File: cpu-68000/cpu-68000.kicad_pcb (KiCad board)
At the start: 4 copper layers, 160 x 100 mm, 114 parts, among them J101 Conn_02x04_Odd_Even, J201 Conn_03x32_Row_Letter_First, J502 DB9_Male_MountingHoles, J503 Conn_02x03_Odd_Even, SW501 SW_DIP_x05, SW502 Blue, SW503 Black, U101 ATF22V10C, U102 ATF22V10C, U103 74HC175, U104 74HC05, U201 SN74LVCH16T245, U202 SN74LVCH16T245, U203 SN74LXC8T245, U204 SN74LVC2T45, U205 SN74LVC2T45, U301 MC68000FN, U303 TL7733B, U304 74HC175, U305 ATF22V10C, U306 74HC148, U401 SST39SF040, U402 SST39SF040, U403 IS61C5128AL-10TLI, U404 IS61C5128AL-10TLI, U501 74HC14, U502 74HC245, U503 XR68C681, U504 PCF8584, U505 DS1744, U506 MAX202, X101 10MHz, Y501 3.6864MHz

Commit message: Placed most items on pcb
- Laid out most components where they should go on the board; mostly
  routed the connector side of the bus buffers and the address bus

- Added 3d models for PLCC sockets, RTC clock module
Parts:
- removed R101: 1k, Resistor_SMD:R_0805_2012Metric
- removed R202: 5k, Resistor_SMD:R_0805_2012Metric
- added R507: 10k, Resistor_SMD:R_0805_2012Metric, F.Cu at (168.2, 107.5)
- added TP201: TestPoint, TestPoint:TestPoint_Loop_D2.60mm_Drill1.4mm_Beaded, F.Cu at (55.2, 115.0)
- added TP202: TestPoint, TestPoint:TestPoint_Loop_D2.60mm_Drill1.4mm_Beaded, F.Cu at (60.7, 115.0)
- D201: value LED_Dual_AAKK -> Grn; footprint 68komputer-common:H201Cxx -> 68komputer-common:H100Cxx
- RN501: footprint Resistor_THT:R_Array_SIP8 -> Resistor_SMD:R_Array_Convex_4x1206
- RN502: value 10k -> R_Network05; footprint Resistor_THT:R_Array_SIP9 -> Resistor_THT:R_Array_SIP6
- U401, U402: value SST39SF040 -> SST39SF040-55-4C; footprint Package_LCC:PLCC-32_THT-Socket -> Package_SO:TSOP-I-32_11.8x8mm_P0.5mm
- moved U505 259.7 mm to (121.5, 108.8), turned to 90 degrees
- moved R201 252.5 mm to (168.9, 28.5)
- moved C505 251.0 mm to (165.2, 127.0)
- moved C509 251.0 mm to (160.8, 127.0)
- moved C506 251.0 mm to (165.2, 124.0)
- moved C507 251.0 mm to (160.8, 124.0)
- moved C508 232.5 mm to (153.3, 123.9)
- moved C510 232.5 mm to (153.3, 126.9)
- moved RN502 228.8 mm to (166.5, 59.2), turned to -90 degrees
- moved C511 228.8 mm to (142.9, 125.3)
- moved Y501 225.7 mm to (120.0, 79.8), turned to 90 degrees
- moved R501 224.3 mm to (148.6, 125.8)
- moved R502 221.0 mm to (138.2, 124.2)
- moved C503 220.1 mm to (124.3, 80.7), turned to 90 degrees
- moved U503 219.0 mm to (136.7, 80.2), turned to 180 degrees
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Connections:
- D201 pad 1: Net-(D201-Pad1) -> GND
- J201 pad a10: /Backplane Connection/BD1 -> GND
- J201 pad a11: /Backplane Connection/BD2 -> /Backplane Connection/BD14
- J201 pad a12: /Backplane Connection/BD3 -> GND
- J201 pad a13: GND -> /Backplane Connection/BA23
- J201 pad a14: /Backplane Connection/BD4 -> GND
- J201 pad a15: /Backplane Connection/BD5 -> /Backplane Connection/BA20
- J201 pad a16: /Backplane Connection/BD6 -> /Backplane Connection/BA13
- J201 pad a17: /Backplane Connection/BD7 -> /Backplane Connection/BA14
- J201 pad a18: GND -> /Backplane Connection/BA11
- J201 pad a19: unconnected-(J201-Pada19) -> GND
- J201 pad a20: unconnected-(J201-Pada20) -> /Backplane Connection/BA7
- J201 pad a21: unconnected-(J201-Pada21) -> /Backplane Connection/BA5
- J201 pad a22: unconnected-(J201-Pada22) -> /Backplane Connection/BR/~{W}
- J201 pad a23: /Backplane Connection/BA1 -> unconnected-(J201-Pada23)
- J201 pad a24: /Backplane Connection/BA3 -> unconnected-(J201-Pada24)
- J201 pad a25: GND -> unconnected-(J201-Pada25)
- J201 pad a26: /Backplane Connection/BA8 -> unconnected-(J201-Pada26)
- J201 pad a27: /Backplane Connection/BA11 -> unconnected-(J201-Pada27)
- J201 pad a28: /Backplane Connection/BA13 -> unconnected-(J201-Pada28)
- J201 pad a29: /Backplane Connection/BA15 -> unconnected-(J201-Pada29)
- J201 pad a3: GND -> /I2C_SCL
- J201 pad a30: GND -> unconnected-(J201-Pada30)
- J201 pad a31: /Backplane Connection/BA18 -> /~{RESET}
- J201 pad a32: /Backplane Connection/BA21 -> /~{IACK_EXT}
- J201 pad a4: /~{BR} -> GND
- J201 pad a5: /I2C_SCL -> GND
- J201 pad a6: /~{IRQ_EXT} -> /Backplane Connection/BD2
- J201 pad a7: /Backplane Connection/BR/~{W} -> /Backplane Connection/BD5
- J201 pad a8: GND -> /Backplane Connection/BD8
- J201 pad a9: /Backplane Connection/BD0 -> /Backplane Connection/BD10
- J201 pad b10: /Backplane Connection/BD10 -> /Backplane Connection/BD12
- J201 pad b11: /Backplane Connection/BD11 -> /Backplane Connection/BD15
- J201 pad b13: /Backplane Connection/BD12 -> GND
- J201 pad b14: /Backplane Connection/BD13 -> /Backplane Connection/BA21
- J201 pad b15: /Backplane Connection/BD14 -> /Backplane Connection/BA15
- J201 pad b16: /Backplane Connection/BD15 -> /Backplane Connection/BA16
- J201 pad b17: GND -> /Backplane Connection/BA10
- J201 pad b18: unconnected-(J201-Padb18) -> GND
- J201 pad b19: unconnected-(J201-Padb19) -> /Backplane Connection/BA9
- J201 pad b20: unconnected-(J201-Padb20) -> /Backplane Connection/BA4
- J201 pad b21: unconnected-(J201-Padb21) -> /Backplane Connection/BA3
- J201 pad b22: unconnected-(J201-Padb22) -> /Backplane Connection/~{BAS}
- J201 pad b24: GND -> unconnected-(J201-Padb24)
- J201 pad b25: /Backplane Connection/BA5 -> unconnected-(J201-Padb25)
- J201 pad b26: /Backplane Connection/BA7 -> unconnected-(J201-Padb26)
- J201 pad b27: /Backplane Connection/BA10 -> unconnected-(J201-Padb27)
- J201 pad b28: /Backplane Connection/BA12 -> unconnected-(J201-Padb28)
- J201 pad b29: GND -> unconnected-(J201-Padb29)
- J201 pad b30: /Backplane Connection/BA17 -> unconnected-(J201-Padb30)
- J201 pad b31: /Backplane Connection/BA19 -> GND
- J201 pad b32: /Backplane Connection/BA22 -> /~{IRQ_EXT}
- J201 pad b4: /~{BG} -> GND
- J201 pad b5: /~{EXT_BERR} -> /Backplane Connection/BD0
- J201 pad b6: /~{RESET} -> /Backplane Connection/BD3
- J201 pad b7: GND -> /Backplane Connection/BD6
- J201 pad b8: /Backplane Connection/BD8 -> /Backplane Connection/BD9
- J201 pad b9: /Backplane Connection/BD9 -> GND
- J201 pad c10: /~{DTACK} -> /Backplane Connection/BD13
- J201 pad c12: unconnected-(J201-Padc12) -> /Backplane Connection/BA22
- J201 pad c13: unconnected-(J201-Padc13) -> /Backplane Connection/BA19
- J201 pad c14: unconnected-(J201-Padc14) -> /Backplane Connection/BA17
- J201 pad c15: unconnected-(J201-Padc15) -> /Backplane Connection/BA18
- J201 pad c16: unconnected-(J201-Padc16) -> /Backplane Connection/BA12
- J201 pad c17: unconnected-(J201-Padc17) -> GND
- J201 pad c18: unconnected-(J201-Padc18) -> /Backplane Connection/BA8
- J201 pad c19: unconnected-(J201-Padc19) -> /Backplane Connection/BA6
- J201 pad c20: unconnected-(J201-Padc20) -> /Backplane Connection/BA2
- J201 pad c21: unconnected-(J201-Padc21) -> /Backplane Connection/BA1
- J201 pad c22: unconnected-(J201-Padc22) -> /Backplane Connection/~{BLDS}
- J201 pad c23: unconnected-(J201-Padc23) -> /Backplane Connection/~{BUDS}
- J201 pad c24: /Backplane Connection/BA2 -> unconnected-(J201-Padc24)
- J201 pad c25: /Backplane Connection/BA4 -> unconnected-(J201-Padc25)
- J201 pad c26: /Backplane Connection/BA6 -> unconnected-(J201-Padc26)
- J201 pad c27: /Backplane Connection/BA9 -> unconnected-(J201-Padc27)
- J201 pad c28: GND -> unconnected-(J201-Padc28)
- J201 pad c29: /Backplane Connection/BA14 -> unconnected-(J201-Padc29)
- J201 pad c3: GND -> /I2C_SDA
- J201 pad c30: /Backplane Connection/BA16 -> unconnected-(J201-Padc30)
- J201 pad c31: /Backplane Connection/BA20 -> /~{DTACK}
- J201 pad c32: /Backplane Connection/BA23 -> /~{EXT_BERR}
- J201 pad c4: /~{BGACK} -> GND
- J201 pad c5: /I2C_SDA -> /Backplane Connection/BD1
- J201 pad c6: /~{IACK_EXT} -> /Backplane Connection/BD4
- J201 pad c7: /Backplane Connection/~{BLDS} -> /Backplane Connection/BD7
- J201 pad c8: /Backplane Connection/~{BUDS} -> GND
- J201 pad c9: /Backplane Connection/~{BAS} -> /Backplane Connection/BD11
- R201 pad 2: Net-(D201-Pad1) -> Net-(D201-Pad2)
- RN301 pad 2: /Main CPU/D7 -> /D7
- RN301 pad 3: /Main CPU/D6 -> /D6
- RN301 pad 4: /Main CPU/D5 -> /D5
- RN301 pad 5: /Main CPU/D4 -> /D4
- RN301 pad 6: /Main CPU/D3 -> /D3
- RN301 pad 7: /Main CPU/D2 -> /D2
- RN301 pad 8: /Main CPU/D1 -> /D1
- RN301 pad 9: /Main CPU/D0 -> /D0
- RN302 pad 2: /Main CPU/D15 -> /D15
- RN302 pad 3: /Main CPU/D14 -> /D14
- RN302 pad 4: /Main CPU/D13 -> /D13
- RN302 pad 5: /Main CPU/D12 -> /D12
- RN302 pad 6: /Main CPU/D11 -> /D11
- RN302 pad 7: /Main CPU/D10 -> /D10
- RN302 pad 8: /Main CPU/D9 -> /D9
- RN302 pad 9: /Main CPU/D8 -> /D8
- RN501 pad 1: Net-(D502-Pad1) -> Net-(D502-Pad2)
- RN501 pad 2: /Peripherals/LED3 -> Net-(D502-Pad1)
- RN501 pad 3: Net-(D502-Pad2) -> Net-(D501-Pad2)
- RN501 pad 4: /Peripherals/LED2 -> Net-(D501-Pad1)
- RN501 pad 5: Net-(D501-Pad2) -> /Peripherals/LED0
- RN501 pad 7: Net-(D501-Pad1) -> /Peripherals/LED2
- RN501 pad 8: /Peripherals/LED0 -> /Peripherals/LED3
- RN502 pad 2: /Peripherals/~{UART_CTS} -> /ROM_REMAP
- RN502 pad 3: unconnected-(RN502-Pad3) -> /Peripherals/DIPSW3
- RN502 pad 4: unconnected-(RN502-Pad4) -> /Peripherals/DIPSW2
- RN502 pad 5: /Peripherals/DIPSW0 -> /Peripherals/DIPSW1
- RN502 pad 6: /Peripherals/DIPSW1 -> /Peripherals/DIPSW0
- SW501 pad 1: /Peripherals/DIPSW0 -> +5V
- SW501 pad 10: +5V -> /Peripherals/DIPSW0
- SW501 pad 2: /Peripherals/DIPSW1 -> +5V
- SW501 pad 3: /Peripherals/DIPSW2 -> +5V
- SW501 pad 4: /Peripherals/DIPSW3 -> +5V
- SW501 pad 5: /ROM_REMAP -> +5V
- SW501 pad 6: +5V -> /ROM_REMAP
- SW501 pad 7: +5V -> /Peripherals/DIPSW3
- SW501 pad 8: +5V -> /Peripherals/DIPSW2
- SW501 pad 9: +5V -> /Peripherals/DIPSW1
- U101 pad 1: /~{UDS} -> unconnected-(U101-Pad1)
- U101 pad 10: unconnected-(U101-Pad10) -> /~{LDS}
- U101 pad 11: unconnected-(U101-Pad11) -> /~{AS}
- U101 pad 13: unconnected-(U101-Pad13) -> /~{UDS}
- U101 pad 2: /~{LDS} -> /~{EXT}
- U101 pad 3: /R/~{W} -> unconnected-(U101-Pad3)
- U101 pad 4: /~{AS} -> unconnected-(U101-Pad4)
- U101 pad 5: /~{MEM_EN} -> unconnected-(U101-Pad5)
- U101 pad 8: unconnected-(U101-Pad8) -> /R/~{W}
- U101 pad 9: unconnected-(U101-Pad9) -> /~{MEM_EN}
- U102 pad 1: /~{MEM_EN} -> unconnected-(U102-Pad1)
- U102 pad 11: unconnected-(U102-Pad11) -> /ROM_REMAP
- U102 pad 14: /~{ROM_CS} -> /~{PERIPH}
- U102 pad 15: /~{RAM_CS} -> /~{ROM_CS}
- U102 pad 16: /~{DUART_CS} -> /~{RAM_CS}
- U102 pad 17: /~{DISP_CS} -> /~{DUART_CS}
- U102 pad 18: /~{NVRAM_CS} -> /~{DISP_CS}
- U102 pad 19: /~{I2C_CS} -> /~{NVRAM_CS}
- U102 pad 20: /DTACK_FAST -> /~{I2C_CS}
- U102 pad 21: /DTACK_SLOW -> /DTACK_FAST
- U102 pad 22: /~{PERIPH} -> /DTACK_SLOW
- U102 pad 23: unconnected-(U102-Pad23) -> /~{EXT}
- U102 pad 6: /A19 -> unconnected-(U102-Pad6)
- U102 pad 8: /ROM_REMAP -> /A19
- U102 pad 9: unconnected-(U102-Pad9) -> /~{MEM_EN}
- U103 pad 10: Net-(J101-Pad4) -> Net-(J101-Pad6)
- U103 pad 12: Net-(J101-Pad6) -> Net-(J101-Pad4)
- U103 pad 13: Net-(J101-Pad4) -> Net-(J101-Pad6)
- U103 pad 15: Net-(J101-Pad2) -> Net-(J101-Pad8)
- U103 pad 2: Net-(J101-Pad8) -> Net-(J101-Pad2)
- U103 pad 5: Net-(J101-Pad8) -> Net-(J101-Pad2)
- U103 pad 7: Net-(J101-Pad6) -> Net-(J101-Pad4)
- U201 pad 11: /Backplane Connection/BD6 -> /Backplane Connection/BD9
- U201 pad 12: /Backplane Connection/BD7 -> /Backplane Connection/BD8
- U201 pad 13: /Backplane Connection/BD8 -> /Backplane Connection/BD7
- U201 pad 14: /Backplane Connection/BD9 -> /Backplane Connection/BD6
- U201 pad 16: /Backplane Connection/BD10 -> /Backplane Connection/BD5
- U201 pad 17: /Backplane Connection/BD11 -> /Backplane Connection/BD4
- U201 pad 19: /Backplane Connection/BD12 -> /Backplane Connection/BD3
- U201 pad 2: /Backplane Connection/BD0 -> /Backplane Connection/BD15
- U201 pad 20: /Backplane Connection/BD13 -> /Backplane Connection/BD2
- U201 pad 22: /Backplane Connection/BD14 -> /Backplane Connection/BD1
- U201 pad 23: /Backplane Connection/BD15 -> /Backplane Connection/BD0
- U201 pad 26: /Backplane Connection/D15 -> /D0
- U201 pad 27: /Backplane Connection/D14 -> /D1
- U201 pad 29: /Backplane Connection/D13 -> /D2
- U201 pad 3: /Backplane Connection/BD1 -> /Backplane Connection/BD14
- U201 pad 30: /Backplane Connection/D12 -> /D3
- U201 pad 32: /Backplane Connection/D11 -> /D4
- U201 pad 33: /Backplane Connection/D10 -> /D5
- U201 pad 35: /Backplane Connection/D9 -> /D6
- U201 pad 36: /Backplane Connection/D8 -> /D7
- U201 pad 37: /Backplane Connection/D7 -> /D8
- U201 pad 38: /Backplane Connection/D6 -> /D9
- U201 pad 40: /Backplane Connection/D5 -> /D10
- U201 pad 41: /Backplane Connection/D4 -> /D11
- U201 pad 43: /Backplane Connection/D3 -> /D12
- U201 pad 44: /Backplane Connection/D2 -> /D13
- U201 pad 46: /Backplane Connection/D1 -> /D14
- U201 pad 47: /Backplane Connection/D0 -> /D15
- U201 pad 5: /Backplane Connection/BD2 -> /Backplane Connection/BD13
- U201 pad 6: /Backplane Connection/BD3 -> /Backplane Connection/BD12
- U201 pad 8: /Backplane Connection/BD4 -> /Backplane Connection/BD11
- U201 pad 9: /Backplane Connection/BD5 -> /Backplane Connection/BD10
- U202 pad 11: /Backplane Connection/BA7 -> /Backplane Connection/BA16
- U202 pad 12: /Backplane Connection/BA8 -> /Backplane Connection/BA13
- U202 pad 13: /Backplane Connection/BA9 -> /Backplane Connection/BA18
- U202 pad 14: /Backplane Connection/BA10 -> /Backplane Connection/BA15
- U202 pad 16: /Backplane Connection/BA11 -> /Backplane Connection/BA20
- U202 pad 17: /Backplane Connection/BA12 -> /Backplane Connection/BA17
- U202 pad 19: /Backplane Connection/BA13 -> /Backplane Connection/BA21
- U202 pad 2: /Backplane Connection/BA1 -> /Backplane Connection/BA9
- U202 pad 20: /Backplane Connection/BA14 -> /Backplane Connection/BA19
- U202 pad 22: /Backplane Connection/BA15 -> /Backplane Connection/BA23
- U202 pad 23: /Backplane Connection/BA16 -> /Backplane Connection/BA22
- U202 pad 26: /Backplane Connection/A16 -> /A22
- U202 pad 27: /Backplane Connection/A15 -> /A23
- U202 pad 29: /Backplane Connection/A14 -> /A19
- U202 pad 3: /Backplane Connection/BA2 -> /Backplane Connection/BA8
- U202 pad 30: /Backplane Connection/A13 -> /A21
- U202 pad 32: /Backplane Connection/A12 -> /A17
- U202 pad 33: /Backplane Connection/A11 -> /A20
- U202 pad 35: /Backplane Connection/A10 -> /A15
- U202 pad 36: /Backplane Connection/A9 -> /A18
- U202 pad 37: /Backplane Connection/A8 -> /A13
- U202 pad 38: /Backplane Connection/A7 -> /A16
- U202 pad 40: /Backplane Connection/A6 -> /A12
- U202 pad 41: /Backplane Connection/A5 -> /A14
- U202 pad 43: /Backplane Connection/A4 -> /A10
- U202 pad 44: /Backplane Connection/A3 -> /A11
- U202 pad 46: /Backplane Connection/A2 -> /A8
- U202 pad 47: /Backplane Connection/A1 -> /A9
- U202 pad 5: /Backplane Connection/BA3 -> /Backplane Connection/BA11
- U202 pad 6: /Backplane Connection/BA4 -> /Backplane Connection/BA10
- U202 pad 8: /Backplane Connection/BA5 -> /Backplane Connection/BA14
- U202 pad 9: /Backplane Connection/BA6 -> /Backplane Connection/BA12
- U203 pad 15: /Backplane Connection/BA23 -> /Backplane Connection/BA1
- U203 pad 16: /Backplane Connection/BA22 -> /Backplane Connection/BA3
- U203 pad 17: /Backplane Connection/BA21 -> /Backplane Connection/BA5
- U203 pad 18: /Backplane Connection/BA20 -> /Backplane Connection/BA2
- U203 pad 19: /Backplane Connection/BA19 -> /Backplane Connection/BA4
- U203 pad 20: /Backplane Connection/BA18 -> /Backplane Connection/BA7
- U203 pad 21: /Backplane Connection/BA17 -> /Backplane Connection/BA6
- U203 pad 3: /Backplane Connection/A17 -> /A6
- U203 pad 4: /Backplane Connection/A18 -> /A7
- U203 pad 5: /Backplane Connection/A19 -> /A4
- U203 pad 6: /Backplane Connection/A20 -> /A2
- U203 pad 7: /Backplane Connection/A21 -> /A5
- U203 pad 8: /Backplane Connection/A22 -> /A3
- U203 pad 9: /Backplane Connection/A23 -> /A1
- U301 pad 1: /Main CPU/D4 -> /D4
- U301 pad 2: /Main CPU/D3 -> /D3
- U301 pad 3: /Main CPU/D2 -> /D2
- U301 pad 32: /Main CPU/A1 -> /A1
- U301 pad 33: /Main CPU/A2 -> /A2
- U301 pad 34: /Main CPU/A3 -> /A3
- U301 pad 35: /Main CPU/A4 -> /A4
- U301 pad 36: /Main CPU/A5 -> /A5
- U301 pad 37: /Main CPU/A6 -> /A6
- U301 pad 38: /Main CPU/A7 -> /A7
- U301 pad 39: /Main CPU/A8 -> /A8
- U301 pad 4: /Main CPU/D1 -> /D1
- U301 pad 40: /Main CPU/A9 -> /A9
- U301 pad 41: /Main CPU/A10 -> /A10
- U301 pad 42: /Main CPU/A11 -> /A11
- U301 pad 43: /Main CPU/A12 -> /A12
- U301 pad 44: /Main CPU/A13 -> /A13
- U301 pad 45: /Main CPU/A14 -> /A14
- U301 pad 46: /Main CPU/A15 -> /A15
- U301 pad 47: /Main CPU/A16 -> /A16
- U301 pad 48: /Main CPU/A17 -> /A17
- U301 pad 49: /Main CPU/A18 -> /A18
- U301 pad 5: /Main CPU/D0 -> /D0
- U301 pad 50: /Main CPU/A19 -> /A19
- U301 pad 51: /Main CPU/A20 -> /A20
- U301 pad 53: /Main CPU/A21 -> /A21
- U301 pad 54: /Main CPU/A22 -> /A22
- U301 pad 55: /Main CPU/A23 -> /A23
- U301 pad 58: /Main CPU/D15 -> /D15
- U301 pad 59: /Main CPU/D14 -> /D14
- U301 pad 60: /Main CPU/D13 -> /D13
- U301 pad 61: /Main CPU/D12 -> /D12
- U301 pad 62: /Main CPU/D11 -> /D11
- U301 pad 63: /Main CPU/D10 -> /D10
- U301 pad 64: /Main CPU/D9 -> /D9
- U301 pad 65: /Main CPU/D8 -> /D8
- U301 pad 66: /Main CPU/D7 -> /D7
- U301 pad 67: /Main CPU/D6 -> /D6
- U301 pad 68: /Main CPU/D5 -> /D5
- U305 pad 1: /Main CPU/A1 -> /~{EXT_BERR}
- U305 pad 10: /Main CPU/FC0 -> /Main CPU/FC1
- U305 pad 11: /Main CPU/FC1 -> /Main CPU/BUS_TIMEOUT
- U305 pad 16: unconnected-(U305-Pad16) -> /~{MEM_EN}
- U305 pad 17: unconnected-(U305-Pad17) -> /~{IACK_DUART}
- U305 pad 18: /Main CPU/~{BERR} -> /~{IACK_I2C}
- U305 pad 19: /~{MEM_EN} -> unconnected-(U305-Pad19)
- U305 pad 2: /Main CPU/A2 -> /A1
- U305 pad 20: /~{IACK_EXT} -> unconnected-(U305-Pad20)
- U305 pad 21: /~{IACK_I2C} -> /Main CPU/~{VPA}
- U305 pad 22: /~{IACK_DUART} -> /Main CPU/~{BERR}
- U305 pad 23: /Main CPU/~{VPA} -> /~{IACK_EXT}
- U305 pad 3: /Main CPU/A3 -> /A2
- U305 pad 4: /Main CPU/A16 -> /A3
- U305 pad 5: /Main CPU/A17 -> /A16
- U305 pad 6: /Main CPU/A18 -> /A17
- U305 pad 7: /Main CPU/A19 -> /A18
- U305 pad 8: /~{EXT_BERR} -> /A19
- U305 pad 9: /Main CPU/BUS_TIMEOUT -> /Main CPU/FC0
- U401 pad 1: /RAM and ROM/A19 -> /A12
- U401 pad 10: /RAM and ROM/A3 -> /A17
- U401 pad 11: /RAM and ROM/A2 -> /A16
- U401 pad 12: /RAM and ROM/A1 -> /A13
- U401 pad 13: /RAM and ROM/D0 -> /A8
- U401 pad 14: /RAM and ROM/D1 -> /A7
- U401 pad 15: /RAM and ROM/D2 -> /A6
- U401 pad 16: GND -> /A5
- U401 pad 17: /RAM and ROM/D3 -> /A4
- U401 pad 18: /RAM and ROM/D4 -> /A3
- U401 pad 19: /RAM and ROM/D5 -> /A2
- U401 pad 2: /RAM and ROM/A17 -> /A10
- U401 pad 20: /RAM and ROM/D6 -> /A1
- U401 pad 21: /RAM and ROM/D7 -> /D0
- U401 pad 22: /~{ROM_CS} -> /D1
- U401 pad 23: /RAM and ROM/A11 -> /D2
- U401 pad 24: /~{LWE} -> GND
- U401 pad 25: /RAM and ROM/A12 -> /D3
- U401 pad 26: /RAM and ROM/A10 -> /D4
- U401 pad 27: /RAM and ROM/A9 -> /D5
- U401 pad 28: /RAM and ROM/A14 -> /D6
- U401 pad 29: /RAM and ROM/A15 -> /D7
- U401 pad 3: /RAM and ROM/A16 -> /A9
- U401 pad 30: /RAM and ROM/A18 -> /~{ROM_CS}
- U401 pad 31: /~{LOE} -> /A11
- U401 pad 32: +5V -> /~{LWE}
- U401 pad 4: /RAM and ROM/A13 -> /A14
- U401 pad 5: /RAM and ROM/A8 -> /A15
- U401 pad 6: /RAM and ROM/A7 -> /A18
- U401 pad 7: /RAM and ROM/A6 -> /~{LOE}
- U401 pad 8: /RAM and ROM/A5 -> +5V
- U401 pad 9: /RAM and ROM/A4 -> /A19
- U402 pad 1: /RAM and ROM/A19 -> /A12
- U402 pad 10: /RAM and ROM/A3 -> /A17
- U402 pad 11: /RAM and ROM/A2 -> /A16
- U402 pad 12: /RAM and ROM/A1 -> /A13
- U402 pad 13: /RAM and ROM/D8 -> /A8
- U402 pad 14: /RAM and ROM/D9 -> /A7
- U402 pad 15: /RAM and ROM/D10 -> /A6
- U402 pad 16: GND -> /A5
- U402 pad 17: /RAM and ROM/D11 -> /A4
- U402 pad 18: /RAM and ROM/D12 -> /A3
- U402 pad 19: /RAM and ROM/D13 -> /A2
- U402 pad 2: /RAM and ROM/A17 -> /A10
- U402 pad 20: /RAM and ROM/D14 -> /A1
- U402 pad 21: /RAM and ROM/D15 -> /D8
- U402 pad 22: /~{ROM_CS} -> /D9
- U402 pad 23: /RAM and ROM/A11 -> /D10
- U402 pad 24: /~{UWE} -> GND
- U402 pad 25: /RAM and ROM/A12 -> /D11
- U402 pad 26: /RAM and ROM/A10 -> /D12
- U402 pad 27: /RAM and ROM/A9 -> /D13
- U402 pad 28: /RAM and ROM/A14 -> /D14
- U402 pad 29: /RAM and ROM/A15 -> /D15
- U402 pad 3: /RAM and ROM/A16 -> /A9
- U402 pad 30: /RAM and ROM/A18 -> /~{ROM_CS}
- U402 pad 31: /~{UOE} -> /A11
- U402 pad 32: +5V -> /~{UWE}
- U402 pad 4: /RAM and ROM/A13 -> /A14
- U402 pad 5: /RAM and ROM/A8 -> /A15
- U402 pad 6: /RAM and ROM/A7 -> /A18
- U402 pad 7: /RAM and ROM/A6 -> /~{UOE}
- U402 pad 8: /RAM and ROM/A5 -> +5V
- U402 pad 9: /RAM and ROM/A4 -> /A19
- U403 pad 10: /RAM and ROM/D1 -> /D1
- U403 pad 13: /RAM and ROM/D2 -> /D2
- U403 pad 14: /RAM and ROM/D3 -> /D3
- U403 pad 16: /RAM and ROM/A6 -> /A6
- U403 pad 17: /RAM and ROM/A7 -> /A7
- U403 pad 18: /RAM and ROM/A8 -> /A8
- U403 pad 19: /RAM and ROM/A9 -> /A9
- U403 pad 20: /RAM and ROM/A10 -> /A10
- U403 pad 26: /RAM and ROM/A11 -> /A11
- U403 pad 27: /RAM and ROM/A12 -> /A12
- U403 pad 28: /RAM and ROM/A13 -> /A13
- U403 pad 29: /RAM and ROM/A14 -> /A14
- U403 pad 3: /RAM and ROM/A1 -> /A1
- U403 pad 30: /RAM and ROM/A15 -> /A15
- U403 pad 31: /RAM and ROM/D4 -> /D4
- U403 pad 32: /RAM and ROM/D5 -> /D5
- U403 pad 35: /RAM and ROM/D6 -> /D6
- U403 pad 36: /RAM and ROM/D7 -> /D7
- U403 pad 38: /RAM and ROM/A16 -> /A16
- U403 pad 39: /RAM and ROM/A17 -> /A17
- U403 pad 4: /RAM and ROM/A2 -> /A2
- U403 pad 40: /RAM and ROM/A18 -> /A18
- U403 pad 41: /RAM and ROM/A19 -> /A19
- U403 pad 5: /RAM and ROM/A3 -> /A3
- U403 pad 6: /RAM and ROM/A4 -> /A4
- U403 pad 7: /RAM and ROM/A5 -> /A5
- U403 pad 9: /RAM and ROM/D0 -> /D0
- U404 pad 10: /RAM and ROM/D9 -> /D9
- U404 pad 13: /RAM and ROM/D10 -> /D10
- U404 pad 14: /RAM and ROM/D11 -> /D11
- U404 pad 16: /RAM and ROM/A6 -> /A6
- U404 pad 17: /RAM and ROM/A7 -> /A7
- U404 pad 18: /RAM and ROM/A8 -> /A8
- U404 pad 19: /RAM and ROM/A9 -> /A9
- U404 pad 20: /RAM and ROM/A10 -> /A10
- U404 pad 26: /RAM and ROM/A11 -> /A11
- U404 pad 27: /RAM and ROM/A12 -> /A12
- U404 pad 28: /RAM and ROM/A13 -> /A13
- U404 pad 29: /RAM and ROM/A14 -> /A14
- U404 pad 3: /RAM and ROM/A1 -> /A1
- U404 pad 30: /RAM and ROM/A15 -> /A15
- U404 pad 31: /RAM and ROM/D12 -> /D12
- U404 pad 32: /RAM and ROM/D13 -> /D13
- U404 pad 35: /RAM and ROM/D14 -> /D14
- U404 pad 36: /RAM and ROM/D15 -> /D15
- U404 pad 38: /RAM and ROM/A16 -> /A16
- U404 pad 39: /RAM and ROM/A17 -> /A17
- U404 pad 4: /RAM and ROM/A2 -> /A2
- U404 pad 40: /RAM and ROM/A18 -> /A18
- U404 pad 41: /RAM and ROM/A19 -> /A19
- U404 pad 5: /RAM and ROM/A3 -> /A3
- U404 pad 6: /RAM and ROM/A4 -> /A4
- U404 pad 7: /RAM and ROM/A5 -> /A5
- U404 pad 9: /RAM and ROM/D8 -> /D8
- U501 pad 12: unconnected-(U501-Pad12) -> /~{NMI}
- U501 pad 13: GND -> Net-(C517-Pad1)
- U501 pad 2: /Peripherals/~{MRES} -> /~{MRES}
- U501 pad 3: Net-(C517-Pad1) -> GND
- U501 pad 4: /Peripherals/~{NMI} -> unconnected-(U501-Pad4)
- U502 pad 2: /Peripherals/D0 -> /D0
- U502 pad 3: /Peripherals/D1 -> /D1
- U502 pad 4: /Peripherals/D2 -> /D2
- U502 pad 5: /Peripherals/D3 -> /D3
- U502 pad 6: /Peripherals/D4 -> /D4
- U502 pad 7: /Peripherals/D5 -> /D5
- U502 pad 8: /Peripherals/D6 -> /D6
- U502 pad 9: /Peripherals/D7 -> /D7
- U503 pad 2: /Peripherals/A1 -> /A1
- U503 pad 4: /Peripherals/A2 -> /A2
- U503 pad 6: /Peripherals/A3 -> /A3
- U503 pad 7: /Peripherals/A4 -> /A4
- U504 pad 6: /Peripherals/A1 -> /A1
- U505 pad 1: /Peripherals/A15 -> /A15
- U505 pad 10: /Peripherals/A1 -> /A1
- U505 pad 2: /Peripherals/A13 -> /A13
- U505 pad 21: /Peripherals/A11 -> /A11
- U505 pad 23: /Peripherals/A12 -> /A12
- U505 pad 24: /Peripherals/A10 -> /A10
- U505 pad 25: /Peripherals/A9 -> /A9
- U505 pad 26: /Peripherals/A14 -> /A14
- U505 pad 3: /Peripherals/A8 -> /A8
- U505 pad 4: /Peripherals/A7 -> /A7
- U505 pad 5: /Peripherals/A6 -> /A6
- U505 pad 6: /Peripherals/A5 -> /A5
- U505 pad 7: /Peripherals/A4 -> /A4
- U505 pad 8: /Peripherals/A3 -> /A3
- U505 pad 9: /Peripherals/A2 -> /A2
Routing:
- net GND: track 0.00 -> 60.0 mm, vias 0 -> 38
- net /A19: track 0.00 -> 41.1 mm
- net /A18: track 0.00 -> 39.7 mm
- net +5V: track 0.00 -> 36.0 mm, vias 0 -> 8
- net /A23: track 0.00 -> 34.5 mm
- net /A22: track 0.00 -> 33.3 mm
- net /A21: track 0.00 -> 32.4 mm
- net /A20: track 0.00 -> 29.4 mm
- net /A7: track 0.00 -> 25.7 mm
- net /A17: track 0.00 -> 25.5 mm
- net /A3: track 0.00 -> 24.2 mm
- net /A5: track 0.00 -> 23.3 mm
- net /A15: track 0.00 -> 23.0 mm
- net /A16: track 0.00 -> 22.5 mm
- net /A6: track 0.00 -> 22.4 mm
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- added copper zone on In2.Cu, net +5V
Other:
- board text added: "+5V"
- board text added: "1 2 3 4"
- board text added: "2021 Tristan Seifert tseifert.me/68komputer"
- board text added: "Autoboot"
- board text added: "Clear NVRAM"
- board text added: "GND"
- board text added: "Periph Waitstates"
- board text added: "ROM Remap"
- board text removed: "2021 Tristan Seifert tseifert.me"

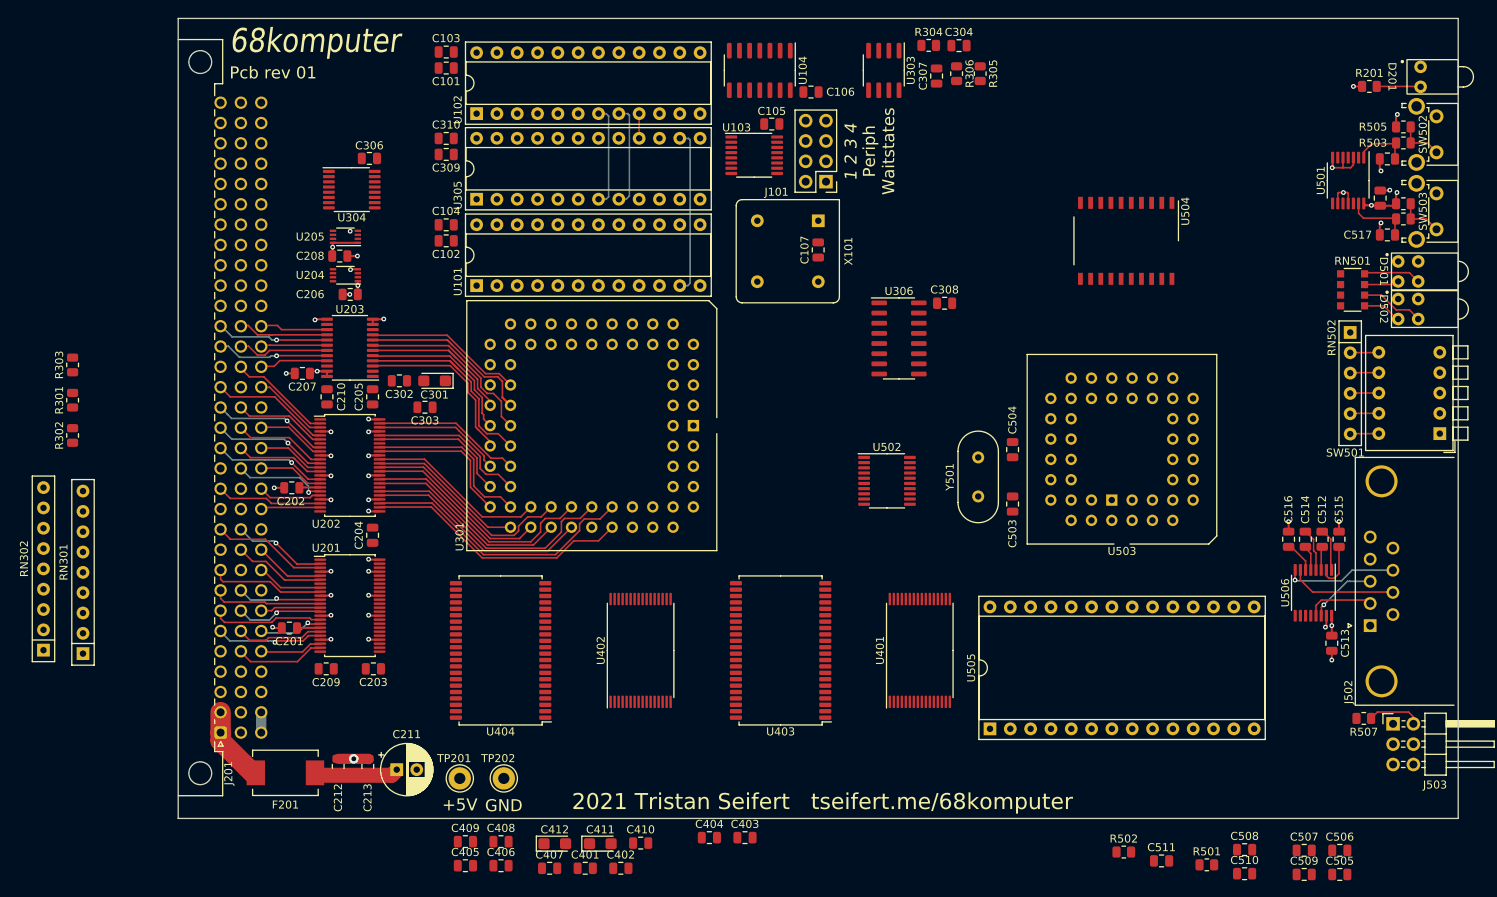
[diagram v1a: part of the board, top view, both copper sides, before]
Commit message: Begin routing stuff
- Routed most control signals to GALs, finished routing signals to bus
  transceivers (except data bus)

- Removed ROMs but doubled up RAM; the boot ROM will be provided by an
  external board

- Added dual SAA1099 chips (audio out via backplane)

- Pullups on some external irq/bus request lines
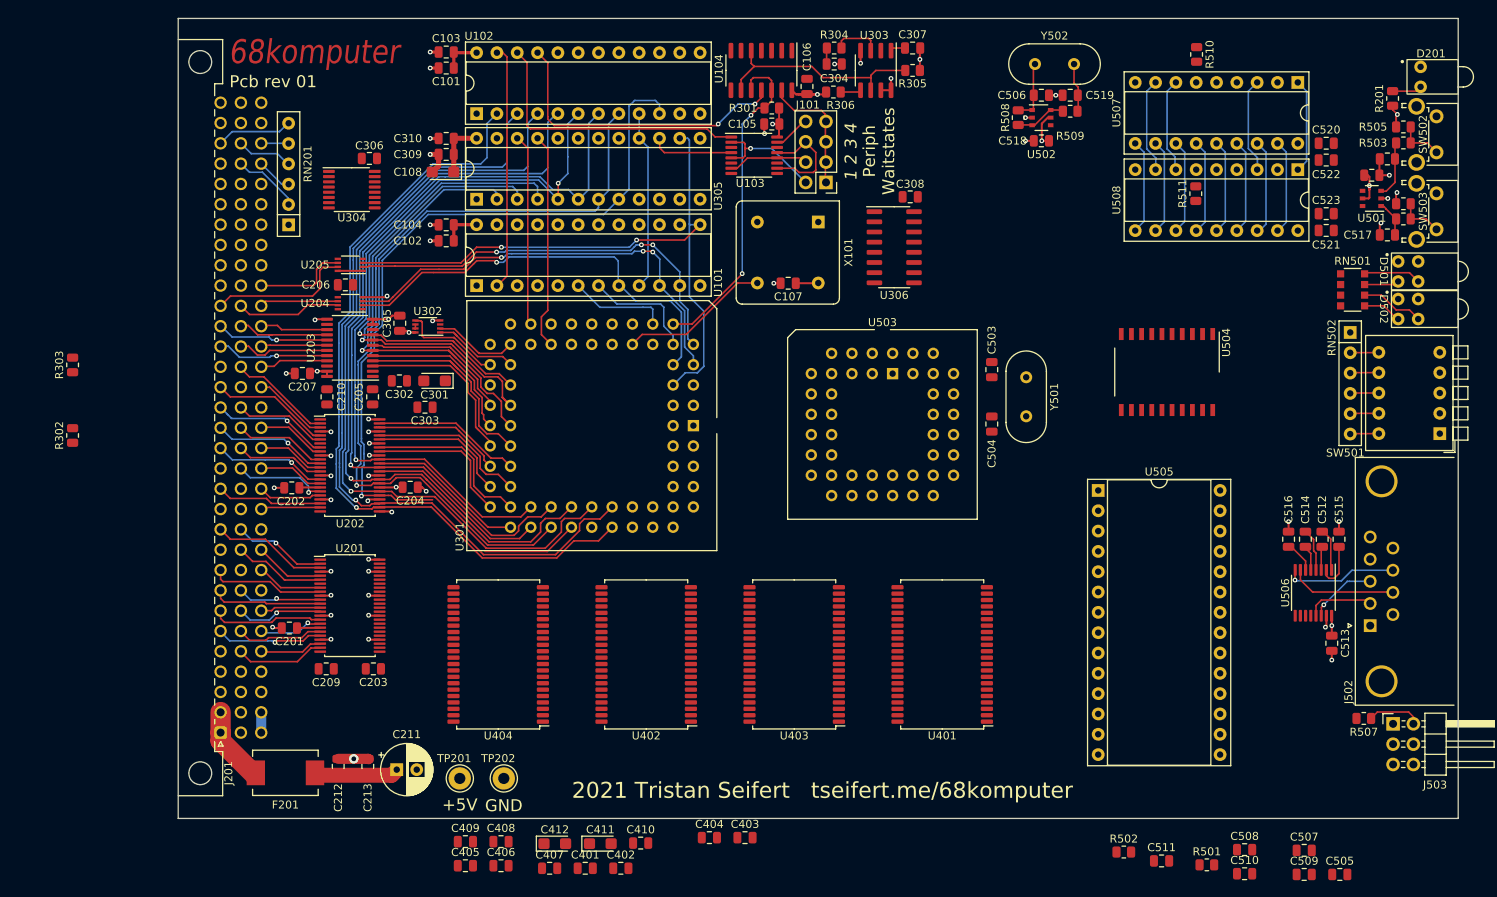
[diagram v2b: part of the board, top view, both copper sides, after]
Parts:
- removed C208: 100nF, Capacitor_SMD:C_0805_2012Metric
- removed RN301, RN302: 10k, Resistor_THT:R_Array_SIP9
- added C108: 10µF, Capacitor_Tantalum_SMD:CP_EIA-3216-18_Kemet-A, F.Cu at (53.1, 39.2)
- added C305: 100nF, Capacitor_SMD:C_0805_2012Metric, F.Cu at (47.7, 58.1)
- added C518: 100nF, Capacitor_SMD:C_0805_2012Metric, F.Cu at (127.9, 35.3)
- added C519: 22pF, Capacitor_SMD:C_0805_2012Metric, F.Cu at (131.5, 29.6)
- added C520: 100nF, Capacitor_SMD:C_0805_2012Metric, F.Cu at (163.5, 35.6)
- added C521: 100nF, Capacitor_SMD:C_0805_2012Metric, F.Cu at (163.5, 46.5)
- added C522: 4.7µF, Capacitor_SMD:C_0805_2012Metric, F.Cu at (163.5, 37.7)
- added C523: 4.7µF, Capacitor_SMD:C_0805_2012Metric, F.Cu at (163.5, 44.4)
- added R508: 200k, Resistor_SMD:R_0805_2012Metric, F.Cu at (125.0, 32.4)
- added R509: 330R, Resistor_SMD:R_0805_2012Metric, F.Cu at (131.5, 31.6)
- added R510: 4k7, Resistor_SMD:R_0805_2012Metric, F.Cu at (147.3, 24.5)
- added R511: 4k7, Resistor_SMD:R_0805_2012Metric, F.Cu at (147.2, 41.9)
- added RN201: 10k, Resistor_THT:R_Array_SIP6, F.Cu at (33.8, 45.8)
- added U302: 74HC2G08DC, Package_SO:VSSOP-8_2.3x2mm_P0.5mm, F.Cu at (51.2, 58.5)
- added U507: SAA1099, Package_DIP:DIP-18_W7.62mm_Socket, F.Cu at (159.9, 28.0)
- added U508: SAA1099, Package_DIP:DIP-18_W7.62mm_Socket, F.Cu at (159.9, 38.9)
- added Y502: 7.15909MHz, Crystal:Crystal_HC49-4H_Vertical, F.Cu at (127.1, 25.7)
- C506: value 100nF -> 22pF
- RN502: value R_Network05 -> 10k
- U401, U402: value SST39SF040-55-4C -> IS61C5128AL-10TLI; footprint Package_SO:TSOP-I-32_11.8x8mm_P0.5mm -> Package_SO:TSOP-II-44_10.16x18.41mm_P0.8mm
- U501: value 74HC14 -> 74HC2G14; footprint Package_SO:TSSOP-14_4.4x5mm_P0.65mm -> Package_SO:TSOP-6_1.65x3.05mm_P0.95mm
- U502: value 74HC245 -> 74HCT2G04; footprint Package_SO:TSSOP-20_4.4x6.5mm_P0.65mm -> Package_SO:TSOP-6_1.65x3.05mm_P0.95mm
- moved C506 101.5 mm to (127.9, 29.6), turned to 180 degrees
- moved R301 94.7 mm to (94.2, 31.2), turned to 180 degrees
- moved U502 49.3 mm to (127.9, 32.4)
- moved U505 32.7 mm to (135.0, 79.0), turned to 0 degrees
- moved U503 31.6 mm to (109.3, 64.4), turned to 0 degrees
- moved U504 17.2 mm to (143.6, 64.2)
- moved C503 17.0 mm to (121.7, 63.9), turned to -90 degrees
- moved Y501 16.1 mm to (126.0, 64.8), turned to -90 degrees
- moved C304 15.8 mm to (102.0, 25.7)
- moved R306 15.6 mm to (101.9, 29.2), turned to 180 degrees
- moved C308 14.0 mm to (111.5, 42.3), turned to 180 degrees
- moved R304 11.8 mm to (102.0, 23.7)
- moved U306 11.4 mm to (109.5, 48.6)
- moved R305 8.46 mm to (111.8, 26.5), turned to 180 degrees
- moved C204 7.62 mm to (49.0, 78.6), turned to 0 degrees
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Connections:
- net /~{RAM_CS} renamed /~{RAM1_CS}
- C506 pad 1: +5V -> GND
- C506 pad 2: GND -> Net-(C506-Pad2)
- J201 pad a29: unconnected-(J201-Pada29) -> /~{RESET}
- J201 pad a30: unconnected-(J201-Pada30) -> /~{IACK_EXT}
- J201 pad a31: /~{RESET} -> GND
- J201 pad a32: /~{IACK_EXT} -> /SNDR
- J201 pad b22: /Backplane Connection/~{BAS} -> /Backplane Connection/~{BLDS}
- J201 pad b23: unconnected-(J201-Padb23) -> /~{DTACK}
- J201 pad b28: unconnected-(J201-Padb28) -> /~{BG}
- J201 pad b29: unconnected-(J201-Padb29) -> /~{BGACK}
- J201 pad b30: unconnected-(J201-Padb30) -> /~{IRQ_EXT}
- J201 pad b32: /~{IRQ_EXT} -> GND
- J201 pad c22: /Backplane Connection/~{BLDS} -> /Backplane Connection/~{BUDS}
- J201 pad c23: /Backplane Connection/~{BUDS} -> /Backplane Connection/~{BAS}
- J201 pad c29: unconnected-(J201-Padc29) -> /~{BR}
- J201 pad c30: unconnected-(J201-Padc30) -> /~{EXT_BERR}
- J201 pad c31: /~{DTACK} -> GND
- J201 pad c32: /~{EXT_BERR} -> /SNDL
- J502 pad 0: unconnected-(J502-Pad0) -> GND
- RN502 pad 2: /ROM_REMAP -> /NO_BERR
- SW501 pad 6: /ROM_REMAP -> /NO_BERR
- U101 pad 10: /~{LDS} -> /~{UDS}
- U101 pad 11: /~{AS} -> /R/~{W}
- U101 pad 13: /~{UDS} -> /~{AS}
- U101 pad 6: /~{BG} -> /~{BGACK}
- U101 pad 7: /~{BGACK} -> /~{BG}
- U101 pad 8: /R/~{W} -> /~{LDS}
- U102 pad 10: unconnected-(U102-Pad10) -> /A19
- U102 pad 11: /ROM_REMAP -> unconnected-(U102-Pad11)
- U102 pad 14: /~{PERIPH} -> /~{SAA1_CS}
- U102 pad 15: /~{ROM_CS} -> /~{SAA2_CS}
- U102 pad 17: /~{DUART_CS} -> /~{RAM2_CS}
- U102 pad 18: /~{DISP_CS} -> /~{DUART_CS}
- U102 pad 2: /A23 -> /A22
- U102 pad 3: /A22 -> /A23
- U102 pad 6: unconnected-(U102-Pad6) -> /A16
- U102 pad 8: /A19 -> /A17
- U103 pad 4: /AS -> AS
- U104 pad 1: /DTACK_FAST -> GND
- U104 pad 10: unconnected-(U104-Pad10) -> /~{DTACK}
- U104 pad 11: GND -> /DTACK_FAST
- U104 pad 12: unconnected-(U104-Pad12) -> /~{DTACK}
- U104 pad 13: GND -> Net-(J101-Pad1)
- U104 pad 2: /~{DTACK} -> unconnected-(U104-Pad2)
- U104 pad 3: Net-(J101-Pad1) -> GND
- U104 pad 4: /~{DTACK} -> unconnected-(U104-Pad4)
- U304 pad 1: /Main CPU/AS -> AS
- U304 pad 4: /Main CPU/AS -> AS
- U305 pad 10: /Main CPU/FC1 -> unconnected-(U305-Pad10)
- U305 pad 13: /Main CPU/FC2 -> unconnected-(U305-Pad13)
- U305 pad 15: /Main CPU/AS -> AS
- U305 pad 19: unconnected-(U305-Pad19) -> /NO_BERR
- U305 pad 2: /A1 -> /A2
- U305 pad 3: /A2 -> /A3
- U305 pad 4: /A3 -> /A1
- U305 pad 6: /A17 -> /A18
- U305 pad 7: /A18 -> /A17
- U305 pad 9: /Main CPU/FC0 -> /Main CPU/CPUSPACE
- U401 pad 1: /A12 -> unconnected-(U401-Pad1)
- U401 pad 10: /A17 -> /D1
- U401 pad 11: /A16 -> +5V
- U401 pad 12: /A13 -> GND
- U401 pad 13: /A8 -> /D2
- U401 pad 14: /A7 -> /D3
- U401 pad 15: /A6 -> /~{LWE}
- U401 pad 16: /A5 -> /A6
- U401 pad 17: /A4 -> /A7
- U401 pad 18: /A3 -> /A8
- U401 pad 19: /A2 -> /A9
- U401 pad 2: /A10 -> unconnected-(U401-Pad2)
- U401 pad 20: /A1 -> /A10
- U401 pad 21: /D0 -> unconnected-(U401-Pad21)
- U401 pad 22: /D1 -> unconnected-(U401-Pad22)
- U401 pad 23: /D2 -> unconnected-(U401-Pad23)
- U401 pad 24: GND -> unconnected-(U401-Pad24)
- U401 pad 25: /D3 -> unconnected-(U401-Pad25)
- U401 pad 26: /D4 -> /A11
- U401 pad 27: /D5 -> /A12
- U401 pad 28: /D6 -> /A13
- U401 pad 29: /D7 -> /A14
- U401 pad 3: /A9 -> /A1
- U401 pad 30: /~{ROM_CS} -> /A15
- U401 pad 31: /A11 -> /D4
- U401 pad 32: /~{LWE} -> /D5
- U401 pad 4: /A14 -> /A2
- U401 pad 5: /A15 -> /A3
- U401 pad 6: /A18 -> /A4
- U401 pad 7: /~{LOE} -> /A5
- U401 pad 8: +5V -> /~{RAM2_CS}
- U401 pad 9: /A19 -> /D0
- U402 pad 1: /A12 -> unconnected-(U402-Pad1)
- U402 pad 10: /A17 -> /D9
- U402 pad 11: /A16 -> +5V
- U402 pad 12: /A13 -> GND
- U402 pad 13: /A8 -> /D10
- U402 pad 14: /A7 -> /D11
- U402 pad 15: /A6 -> /~{UWE}
- U402 pad 16: /A5 -> /A6
- U402 pad 17: /A4 -> /A7
- U402 pad 18: /A3 -> /A8
- U402 pad 19: /A2 -> /A9
- U402 pad 2: /A10 -> unconnected-(U402-Pad2)
- U402 pad 20: /A1 -> /A10
- U402 pad 21: /D8 -> unconnected-(U402-Pad21)
- U402 pad 22: /D9 -> unconnected-(U402-Pad22)
- U402 pad 23: /D10 -> unconnected-(U402-Pad23)
- U402 pad 24: GND -> unconnected-(U402-Pad24)
- U402 pad 25: /D11 -> unconnected-(U402-Pad25)
- U402 pad 26: /D12 -> /A11
- U402 pad 27: /D13 -> /A12
- U402 pad 28: /D14 -> /A13
- U402 pad 29: /D15 -> /A14
- U402 pad 3: /A9 -> /A1
- U402 pad 30: /~{ROM_CS} -> /A15
- U402 pad 31: /A11 -> /D12
- U402 pad 32: /~{UWE} -> /D13
- U402 pad 4: /A14 -> /A2
- U402 pad 5: /A15 -> /A3
- U402 pad 6: /A18 -> /A4
- U402 pad 7: /~{UOE} -> /A5
- U402 pad 8: +5V -> /~{RAM2_CS}
- U402 pad 9: /A19 -> /D8
- U501 pad 1: Net-(C502-Pad1) -> Net-(C517-Pad1)
- U501 pad 2: /~{MRES} -> GND
- U501 pad 3: GND -> Net-(C502-Pad1)
- U501 pad 4: unconnected-(U501-Pad4) -> /~{MRES}
- U501 pad 5: GND -> +5V
- U501 pad 6: unconnected-(U501-Pad6) -> /~{NMI}
- U502 pad 1: /~{RD} -> Net-(C506-Pad2)
- U502 pad 2: /D0 -> GND
- U502 pad 3: /D1 -> Net-(R508-Pad1)
- U502 pad 4: /D2 -> /Peripherals/SNDCLK
- U502 pad 5: /D3 -> +5V
- U502 pad 6: /D4 -> Net-(R508-Pad1)
- U503 pad 18: /Peripherals/PD1 -> /D1
- U503 pad 19: /Peripherals/PD3 -> /D3
- U503 pad 20: /Peripherals/PD5 -> /D5
- U503 pad 21: /Peripherals/PD7 -> /D7
- U503 pad 25: /Peripherals/PD6 -> /D6
- U503 pad 26: /Peripherals/PD4 -> /D4
- U503 pad 27: /Peripherals/PD2 -> /D2
- U503 pad 28: /Peripherals/PD0 -> /D0
- U504 pad 11: /Peripherals/PD3 -> /D3
- U504 pad 12: /Peripherals/PD4 -> /D4
- U504 pad 13: /Peripherals/PD5 -> /D5
- U504 pad 14: /Peripherals/PD6 -> /D6
- U504 pad 15: /Peripherals/PD7 -> /D7
- U504 pad 7: /Peripherals/PD0 -> /D0
- U504 pad 8: /Peripherals/PD1 -> /D1
- U504 pad 9: /Peripherals/PD2 -> /D2
- U505 pad 11: /Peripherals/PD0 -> /D0
- U505 pad 12: /Peripherals/PD1 -> /D1
- U505 pad 13: /Peripherals/PD2 -> /D2
- U505 pad 15: /Peripherals/PD3 -> /D3
- U505 pad 16: /Peripherals/PD4 -> /D4
- U505 pad 17: /Peripherals/PD5 -> /D5
- U505 pad 18: /Peripherals/PD6 -> /D6
- U505 pad 19: /Peripherals/PD7 -> /D7
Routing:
- net /A17: track 25.5 -> 102.0 mm, vias 0 -> 1
- net /A16: track 22.5 -> 92.6 mm, vias 0 -> 2
- net /A20: track 29.4 -> 98.7 mm, vias 0 -> 1
- net /A21: track 32.4 -> 100.1 mm, vias 0 -> 1
- net /A23: track 34.5 -> 101.4 mm, vias 0 -> 1
- net /A22: track 33.3 -> 98.6 mm, vias 0 -> 1
- net /A18: track 39.7 -> 101.7 mm, vias 0 -> 1
- net /A19: track 41.1 -> 102.4 mm, vias 0 -> 1
- net /~{AS}: track 20.7 -> 80.6 mm, vias 0 -> 2
- net /~{UDS}: track 0.00 -> 55.0 mm, vias 0 -> 3
- net /~{LDS}: track 0.00 -> 54.1 mm, vias 0 -> 1
- net /~{DTACK}: track 0.00 -> 53.2 mm, vias 0 -> 2
- net /R/~{W}: track 0.00 -> 52.4 mm, vias 0 -> 3
- net /A1: track 19.9 -> 70.2 mm, vias 0 -> 1
- net +5V: track 36.0 -> 79.3 mm, vias 8 -> 12
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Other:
- board text added: "Keepout area for card guide"
- board text added: "~{BERR} Inhibit"
- board text removed: "ROM Remap"
